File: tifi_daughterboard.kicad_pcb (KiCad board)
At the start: 2 copper layers, 57.4 x 32.3 mm, 20 parts, among them J1 SSW-110-23-F-D, J2 SSW-110-23-F-D, J3 SM04B-SRSS-TB(LF)(SN), J4 SSW-103-02-T-S-RA, Q1 BSS138LT1G, U1 SGP40-D-R4, U2 SHT40-AD1B-R3

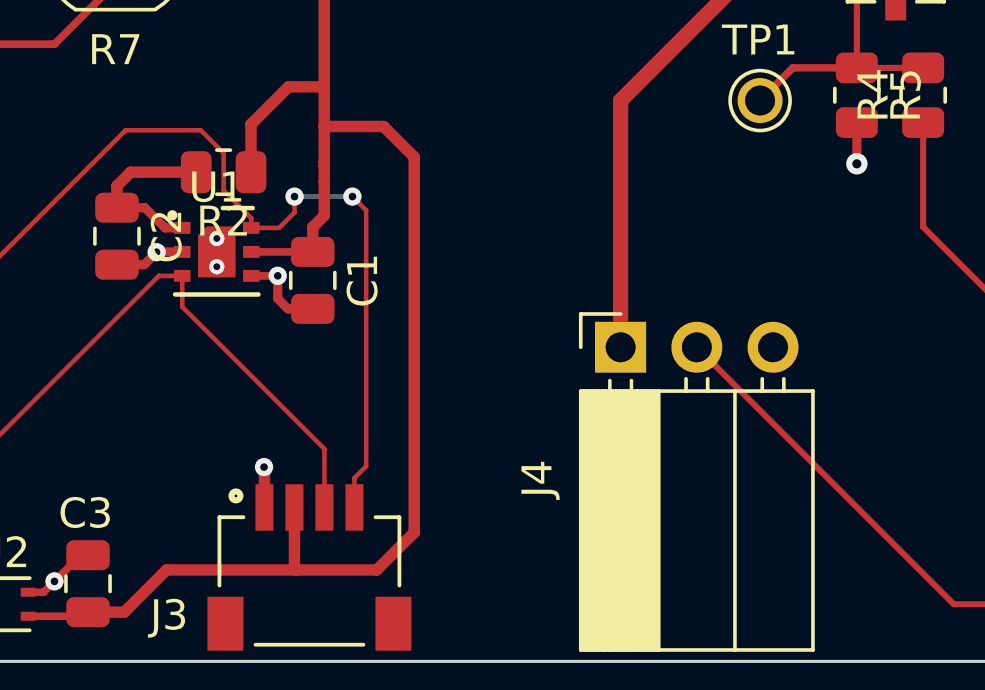
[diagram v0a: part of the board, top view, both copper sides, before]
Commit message: Add TVS diodes to connectors.
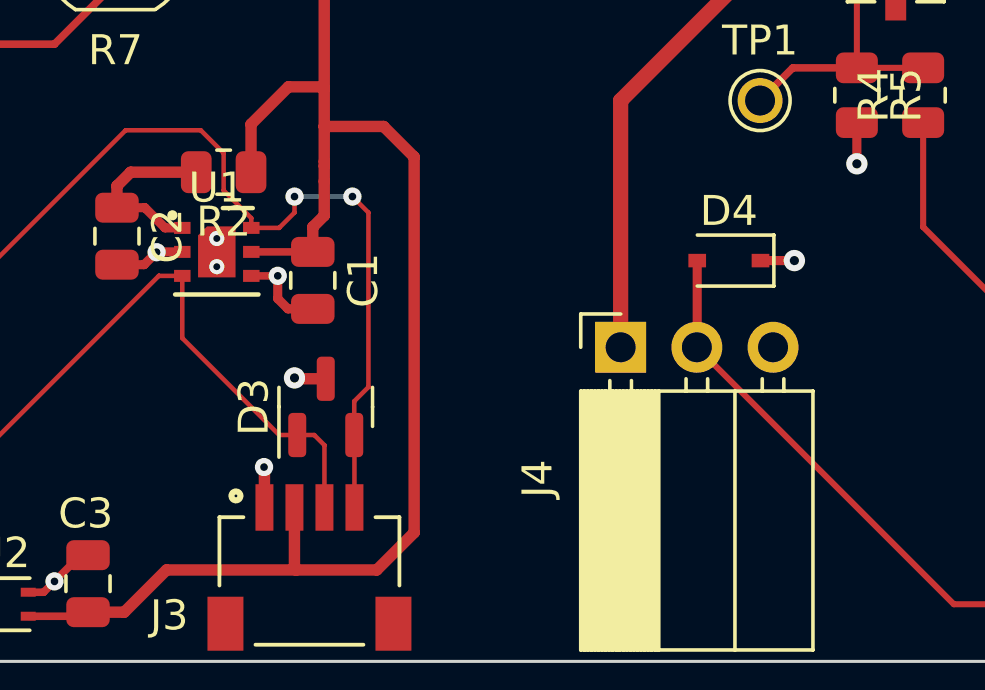
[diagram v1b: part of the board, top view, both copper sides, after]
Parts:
- added D3: SP0502BAHTG, Package_TO_SOT_SMD:SOT-23, F.Cu at (140.3, 93.4)
- added D4: DESD5V0U1BA-7, TiFi Footprints:D_SOD-323, F.Cu at (153.7, 88.5)
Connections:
- U1 pad 7: (no net) -> GND
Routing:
- net PIR_OUT: track 45.0 -> 47.9 mm
- net GND: track 13.0 -> 15.2 mm, vias 9 -> 11
- net I2C_SDA: track 34.6 -> 35.3 mm

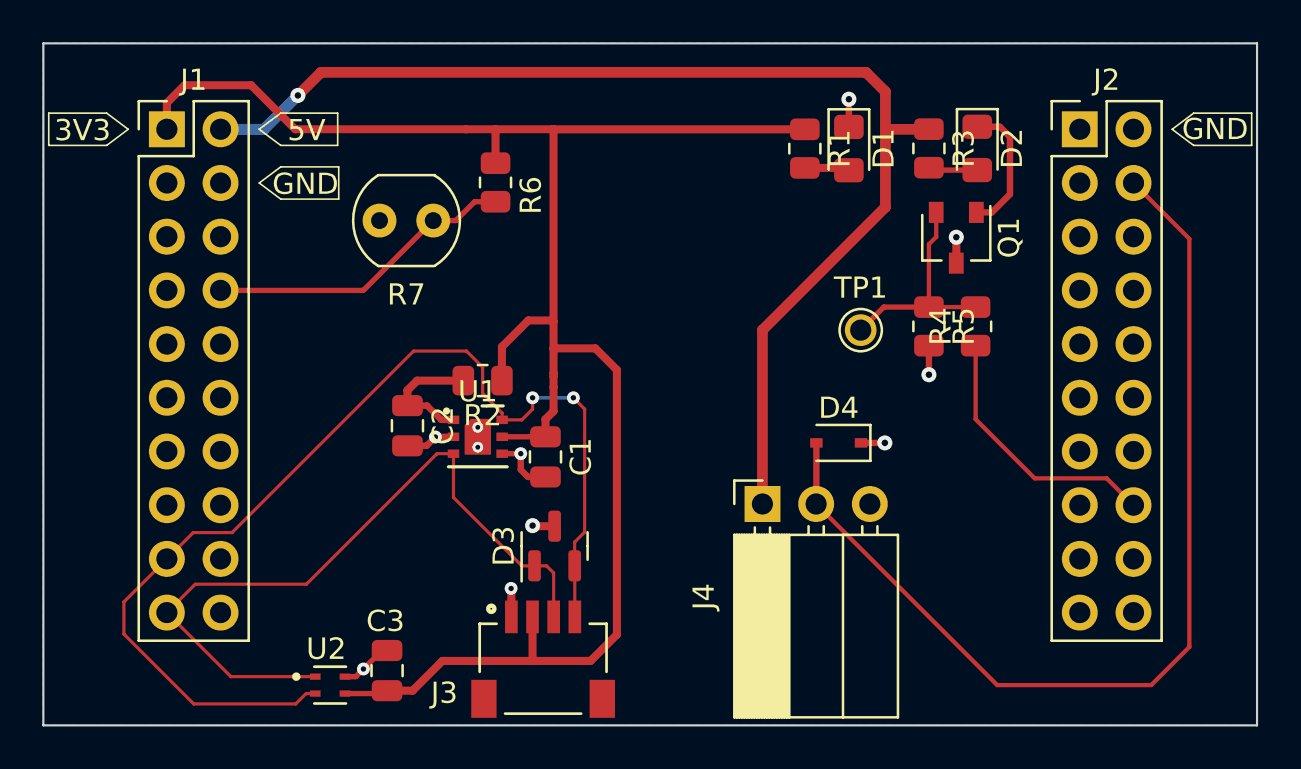
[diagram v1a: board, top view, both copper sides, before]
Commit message: Add useful info to silkscreen layer
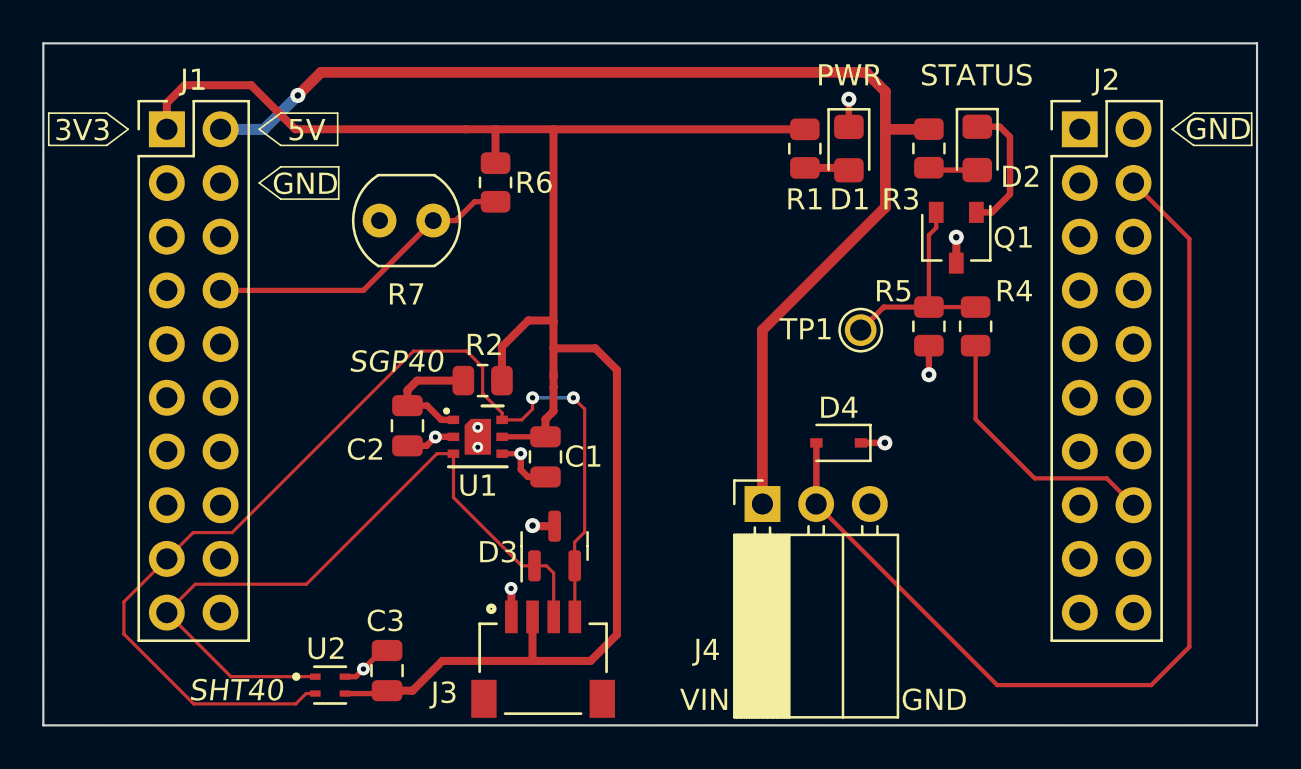
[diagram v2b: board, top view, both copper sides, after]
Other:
- board text added: "PWR"
- board text added: "REV0"
- board text added: "SGP40"
- board text added: "SHT40"
- board text added: "STATUS"
- board text added: "VIN"
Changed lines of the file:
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@@
     (property "Sheetname" "")
     (attr smd)
-    (fp_text reference "D1" (at 0 -1.65 90) (layer "F.SilkS")
+    (fp_text reference "D1" (at 2.4134 -0.0508 180) (layer "F.SilkS")
       (effects (font (size 1 1) (thickness 0.15)))
     )
@@
     (property "Sheetname" "")
     (attr smd)
-    (fp_text reference "R2" (at 0 -1.65) (layer "F.SilkS")
+    (fp_text reference "R2" (at -0.0762 1.6764) (layer "F.SilkS")
       (effects (font (size 1 1) (thickness 0.15)))
     )
@@
     (property "Sheetname" "")
     (attr smd)
-    (fp_text reference "C2" (at 0 -1.68 90) (layer "F.SilkS")
+    (fp_text reference "C2" (at 1.143 1.9812 180) (layer "F.SilkS")
       (effects (font (size 1 1) (thickness 0.15)))
     )
@@
     (property "Sheetname" "")
     (attr smd)
-    (fp_text reference "D2" (at 0 -1.65 90) (layer "F.SilkS")
+    (fp_text reference "D2" (at 1.3552 -2.0574 180) (layer "F.SilkS")
       (effects (font (size 1 1) (thickness 0.15)))
     )
@@
     (property "Sheetname" "")
     (attr smd)
-    (fp_text reference "Q1" (at 0 -2.5 90) (layer "F.SilkS")
+    (fp_text reference "Q1" (at 0 -2.7178 180) (layer "F.SilkS")
       (effects (font (size 1 1) (thickness 0.15)))
     )
@@
     (property "Sheetname" "")
     (attr smd)
-    (fp_text reference "R5" (at 0 -1.65 90) (layer "F.SilkS")
+    (fp_text reference "R5" (at -1.651 1.6764 180) (layer "F.SilkS")
       (effects (font (size 1 1) (thickness 0.15)))
     )
@@
     (property "Sheetname" "")
     (attr smd)
-    (fp_text reference "R4" (at 0 -1.65 90) (layer "F.SilkS")
+    (fp_text reference "R4" (at 1.651 1.8288 180) (layer "F.SilkS")
       (effects (font (size 1 1) (thickness 0.15)))
     )
@@
     (property "Sheetname" "")
     (attr through_hole)
-    (fp_text reference "J4" (at -4.38 -2.77 90) (layer "F.SilkS")
+    (fp_text reference "J4" (at -6.9146 -2.6162 180) (layer "F.SilkS")
       (effects (font (size 1 1) (thickness 0.15)))
     )
@@
     (property "Sheetname" "")
     (attr smd)
-    (fp_text reference "D3" (at 0 -2.4 90) (layer "F.SilkS")
+    (fp_text reference "D3" (at -0.3048 -2.6924 180) (layer "F.SilkS")
       (effects (font (size 1 1) (thickness 0.15)))
     )
@@
     (property "Sheetname" "")
     (attr smd)
-    (fp_text reference "R3" (at 0 -1.65 90) (layer "F.SilkS")
+    (fp_text reference "R3" (at 2.422 1.3208 180) (layer "F.SilkS")
       (effects (font (size 1 1) (thickness 0.15)))
     )
@@
     (property "Sheetname" "")
     (attr smd)
-    (fp_text reference "R1" (at 0 -1.65 90) (layer "F.SilkS")
+    (fp_text reference "R1" (at 2.4134 0 180) (layer "F.SilkS")
       (effects (font (size 1 1) (thickness 0.15)))
     )
@@
     (property "Sheetname" "")
     (attr smd)
-    (fp_text reference "U1" (at 0 -2.14) (layer "F.SilkS")
+    (fp_text reference "U1" (at 0 2.3216) (layer "F.SilkS")
       (effects (font (size 1 1) (thickness 0.15)))
     )
@@
     (property "Sheetname" "")
     (attr smd)
-    (fp_text reference "R6" (at 0.6096 -1.6764 90) (layer "F.SilkS")
+    (fp_text reference "R6" (at 0.0254 -1.8288 180) (layer "F.SilkS")
       (effects (font (size 1 1) (thickness 0.15)))
     )
@@
     (property "Sheetname" "")
     (attr exclude_from_pos_files)
-    (fp_text reference "TP1" (at 0 -1.998) (layer "F.SilkS")
+    (fp_text reference "TP1" (at -2.5654 -0.0254) (layer "F.SilkS")
       (effects (font (size 1 1) (thickness 0.15)))
     )
@@
     (property "Sheetname" "")
     (attr smd)
-    (fp_text reference "C1" (at 0 -1.68 90) (layer "F.SilkS")
+    (fp_text reference "C1" (at 0 -1.8034 180) (layer "F.SilkS")
       (effects (font (size 1 1) (thickness 0.15)))
     )
@@
   (gr_poly
     (pts
+      (xy 126.2888 76.2)
+      (xy 127.3048 76.962)
+      (xy 129.9972 76.962)
+      (xy 129.9972 75.438)
+      (xy 127.3048 75.438)
+    ) (layer "B.SilkS") (width 0.0762) (fill none))
+  (gr_poly
+    (pts
+      (xy 120.096443 73.66)
+      (xy 119.080443 72.898)
+      (xy 116.337243 72.898)
+      (xy 116.337243 74.422)
+      (xy 119.080443 74.422)
+    ) (layer "B.SilkS") (width 0.0762) (fill none))
+  (gr_poly
+    (pts
+      (xy 126.2888 73.66)
+      (xy 127.3048 74.422)
+      (xy 130.048 74.422)
+      (xy 130.048 72.898)
+      (xy 127.3048 72.898)
+    ) (layer "B.SilkS") (width 0.0762) (fill none))
+  (gr_poly
+    (pts
+      (xy 169.4688 73.66)
+      (xy 170.4848 74.422)
+      (xy 173.228 74.422)
+      (xy 173.228 72.898)
+      (xy 170.4848 72.898)
+    ) (layer "B.SilkS") (width 0.0762) (fill none))
+  (gr_poly
+    (pts
       (xy 120.0912 73.66)
       (xy 119.0752 74.422)
@@
     ) (layer "F.SilkS") (width 0.0762) (fill none))
   (gr_rect (start 116.078 69.596) (end 173.482 101.854) (layer "Edge.Cuts") (width 0.1016) (fill none))
+  (gr_text "REV0" (at 170.2562 99.8474) (layer "B.SilkS")
+    (effects (font (size 1 1) (thickness 0.15)) (justify mirror))
+  )
+  (gr_text "GND" (at 128.4732 76.2508) (layer "B.SilkS")
+    (effects (font (size 1 1) (thickness 0.15)) (justify mirror))
+  )
+  (gr_text "5V" (at 128.6256 73.7108) (layer "B.SilkS")
+    (effects (font (size 1 1) (thickness 0.15)) (justify mirror))
+  )
+  (gr_text "3V3" (at 117.8814 73.7108) (layer "B.SilkS")
+    (effects (font (size 1 1) (thickness 0.15)) (justify mirror))
+  )
+  (gr_text "GND" (at 171.6786 73.66) (layer "B.SilkS")
+    (effects (font (size 1 1) (thickness 0.15)) (justify mirror))
+  )
+  (gr_text "GND" (at 158.2166 100.6602) (layer "F.SilkS")
+    (effects (font (size 1 1) (thickness 0.15)))
+  )
+  (gr_text "SHT40" (at 125.1966 100.203) (layer "F.SilkS")
+    (effects (font (size 1 1) (thickness 0.15) italic))
+  )
   (gr_text "GND" (at 128.4732 76.2508) (layer "F.SilkS")
     (effects (font (size 1 1) (thickness 0.15)))
   )
-  (gr_text "GND" (at 171.5008 73.66) (layer "F.SilkS")
+  (gr_text "GND" (at 171.6532 73.66) (layer "F.SilkS")
+    (effects (font (size 1 1) (thickness 0.15)))
+  )
+  (gr_text "PWR" (at 154.2034 71.12) (layer "F.SilkS")
     (effects (font (size 1 1) (thickness 0.15)))
   )
@@
     (effects (font (size 1 1) (thickness 0.15)))
   )
+  (gr_text "SGP40" (at 132.7658 84.6582) (layer "F.SilkS")
+    (effects (font (size 1 1) (thickness 0.15) italic))
+  )
+  (gr_text "STATUS" (at 160.2232 71.12) (layer "F.SilkS")
+    (effects (font (size 1 1) (thickness 0.15)))
+  )
   (gr_text "5V" (at 128.524 73.7108) (layer "F.SilkS")
+    (effects (font (size 1 1) (thickness 0.15)))
+  )
+  (gr_text "VIN" (at 147.3708 100.6602) (layer "F.SilkS")
     (effects (font (size 1 1) (thickness 0.15)))
   )
@@
   (segment (start 166.37 90.17) (end 162.9664 90.17) (width 0.2032) (layer "F.Cu") (net 37))
   (segment (start 162.9664 90.17) (end 160.1724 87.376) (width 0.2032) (layer "F.Cu") (net 37))
-  (segment (start 157.9626 79.0956) (end 158.308 78.7502) (width 0.2032) (layer "F.Cu") (net 42))
   (segment (start 155.8271 82.0693) (end 157.9626 82.0693) (width 0.25) (layer "F.Cu") (net 42))
   (segment (start 154.7368 83.1596) (end 155.8271 82.0693) (width 0.25) (layer "F.Cu") (net 42))
   (segment (start 160.1724 82.0693) (end 157.9626 82.0693) (width 0.2032) (layer "F.Cu") (net 42))
-  (segment (start 157.9626 82.0693) (end 157.9626 79.0956) (width 0.2032) (layer "F.Cu") (net 42))
-  (segment (start 158.308 78.7502) (end 158.308 77.5908) (width 0.2032) (layer "F.Cu") (net 42))
+  (segment (start 157.9626 82.0693) (end 157.9626 78.6638) (width 0.2032) (layer "F.Cu") (net 42))
+  (segment (start 157.9626 78.6638) (end 158.308 78.3184) (width 0.2032) (layer "F.Cu") (net 42))
+  (segment (start 158.308 78.3184) (end 158.308 77.5908) (width 0.2032) (layer "F.Cu") (net 42))
   (segment (start 133.2992 86.0044) (end 133.7564 85.5472) (width 0.381) (layer "F.Cu") (net 43))
   (segment (start 133.2992 86.7308) (end 133.2992 86.0044) (width 0.381) (layer "F.Cu") (net 43))

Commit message: Add optional I2C pullups.
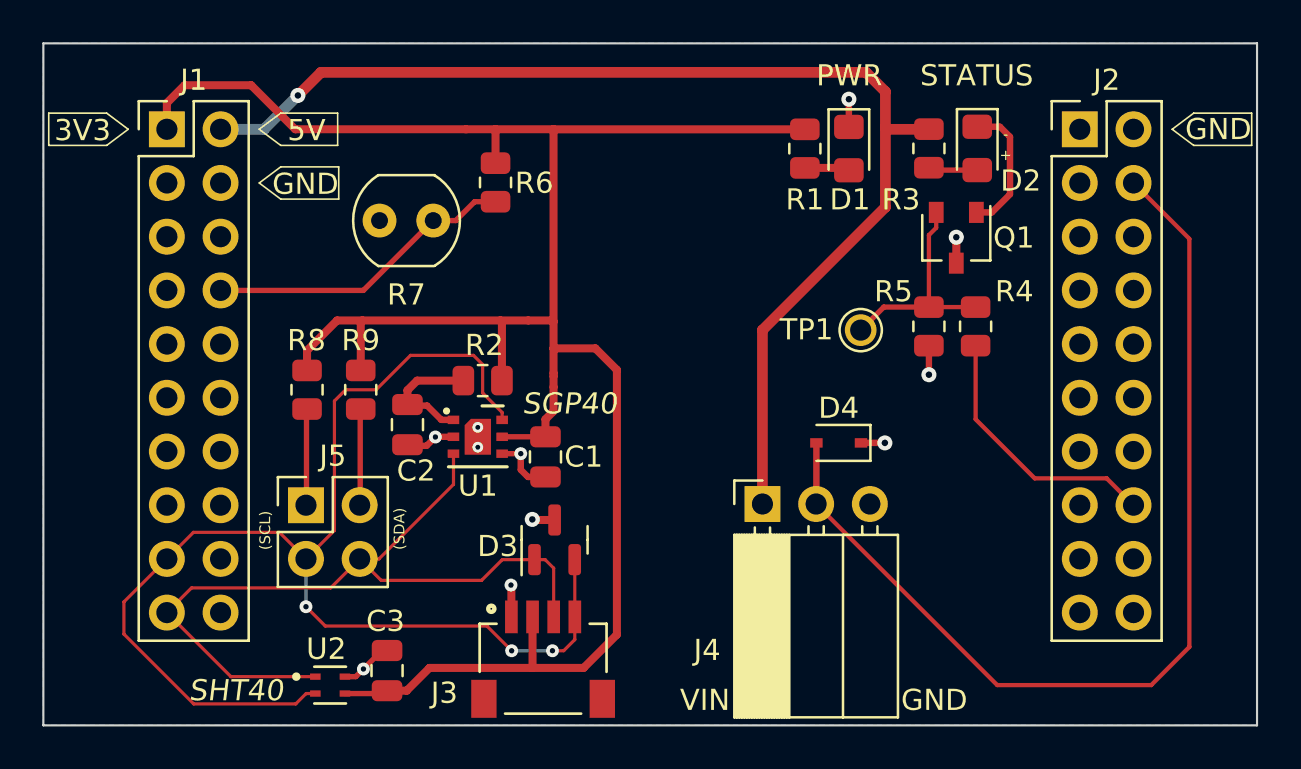
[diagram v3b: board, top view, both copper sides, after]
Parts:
- added J5: PH2-04-UA, Connector_PinHeader_2.54mm:PinHeader_2x02_P2.54mm_Vertical, F.Cu at (128.5, 91.4)
- added R8: 3.3k, Resistor_SMD:R_0805_2012Metric, F.Cu at (128.5, 86.0)
- added R9: 3.3k, Resistor_SMD:R_0805_2012Metric, F.Cu at (131.1, 86.0)
- moved D3 0.29 mm to (140.3, 93.1)
- moved C2 0.05 mm to (133.3, 87.6)
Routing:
- net +3.3V: track 87.4 -> 101.4 mm
- net I2C_SCL: track 52.1 -> 61.6 mm, vias 2 -> 3
- net Net-(J5-Pad2): track 0.00 -> 4.57 mm
- net Net-(J5-Pad1): track 0.00 -> 4.57 mm
- net I2C_SDA: track 35.3 -> 38.3 mm
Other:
- board text added: "(SCL)"
- board text added: "(SDA)"
- board text added: "+"
- board text added: "-"

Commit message: Add logo
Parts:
- added G***: LOGO, TiFi Footprints:logo, F.Cu at (166.3, 100.3)
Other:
- board text added: "TI-FI DAUGHTERBOARD"

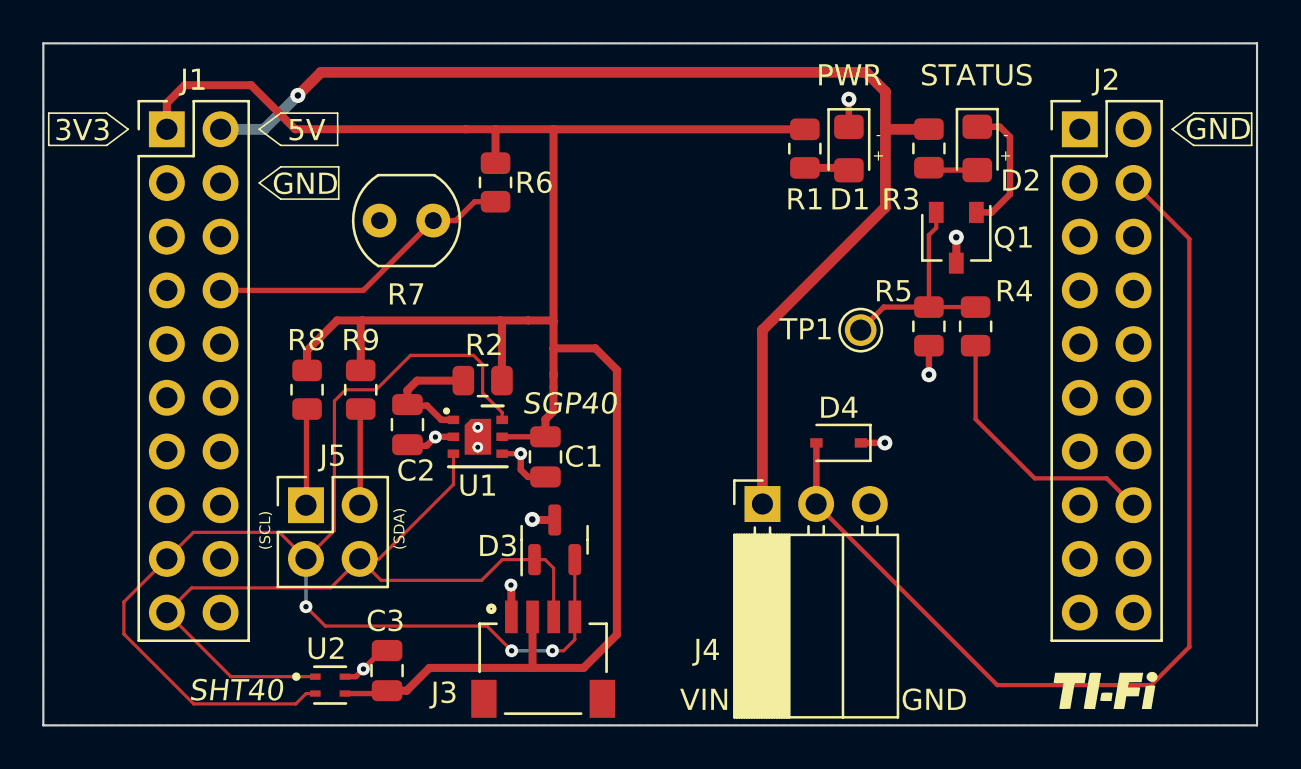
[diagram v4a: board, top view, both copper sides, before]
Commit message: Add mask clearance and supplier link fields.
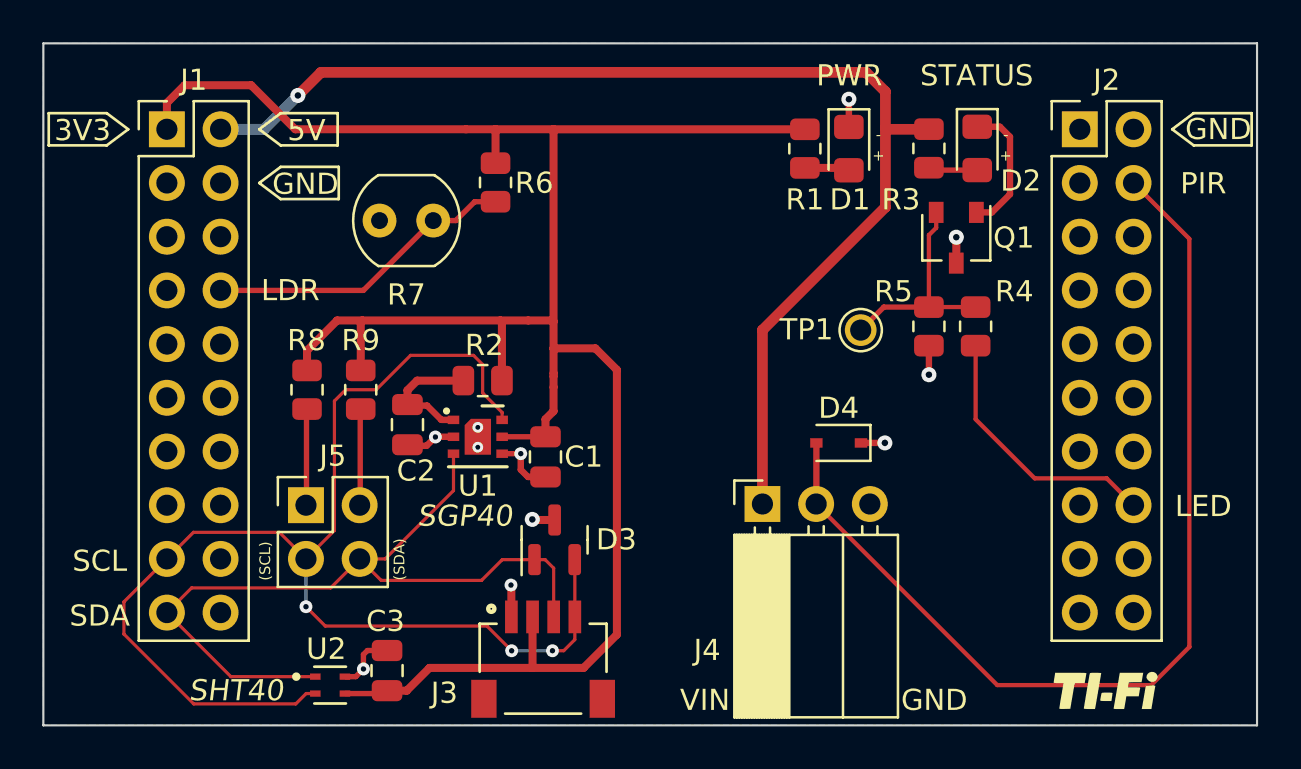
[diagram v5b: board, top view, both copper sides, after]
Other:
- rule pad_to_mask_clearance: 0 -> 0.0635
- board text added: "LDR"
- board text added: "LED"
- board text added: "PIR"
- board text added: "SCL"
- board text added: "SDA"
